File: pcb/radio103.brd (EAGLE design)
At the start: 99 x 98.7 mm, 11 parts, among them IC1 LM833D, IC2 LM833D, IC3 74ACT00D, IC4 MCP23S17SO, IC5 LM386M-1, U1 FST3253

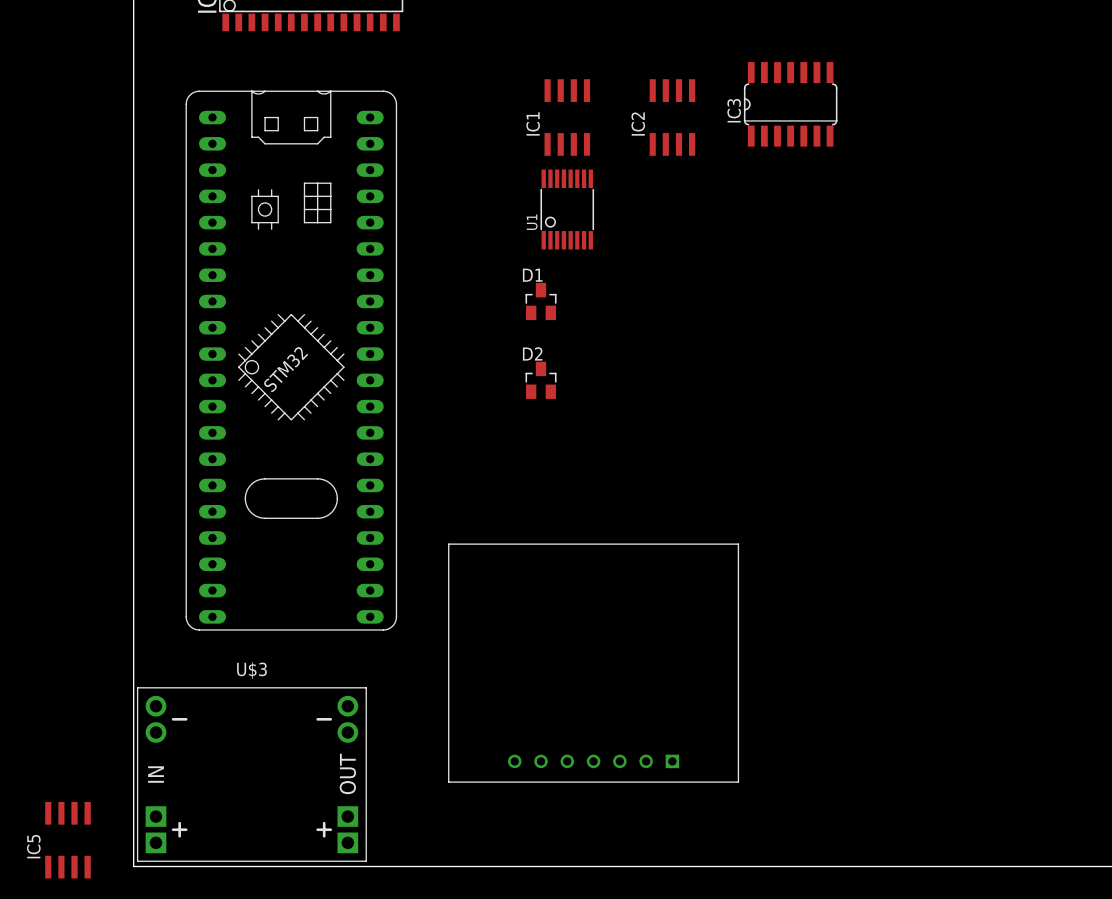
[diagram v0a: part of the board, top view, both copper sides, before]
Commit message: AGC + soft clipper
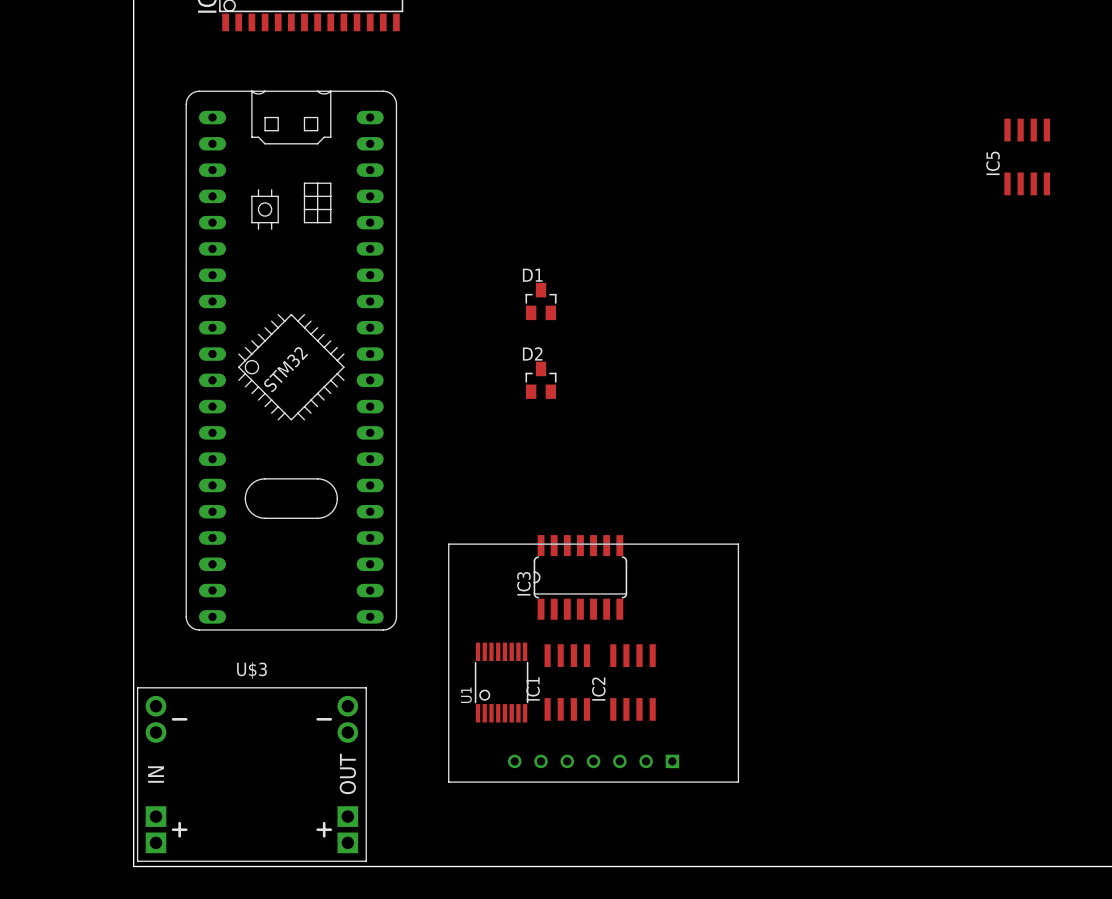
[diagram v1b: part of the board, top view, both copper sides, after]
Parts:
- moved IC5 113.8 mm to (86.4, 68.6)
- moved IC2 54.7 mm to (48.3, 17.8)
- moved IC1 54.6 mm to (41.9, 17.8)
- moved IC3 50.0 mm to (43.2, 27.9)
- moved U1 46.2 mm to (35.6, 17.8)
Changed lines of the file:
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@@
 </layers>
 <board>
+<fusionsync huburn="a.cGVyc29uYWw6dWUyYzhiYjNk" projecturn="a.cGVyc29uYWw6dWUyYzhiYjNkIzIwMTkwMTI3MTcyNzM0MDc2" f3durn="urn:adsk.wipprod:dm.lineage:HAib8JV9QH6EPJWf0lSnAA" pcbguid="9a40abf5-9ee6-4638-9549-066028e06783" lastpulledtime="" lastsyncedchangeguid="" latestrevisionid="0aad2595-9f46-4cf1-a5a6-6076ba2b8e60" lastsyncedrevisionid="0aad2595-9f46-4cf1-a5a6-6076ba2b8e60" lastboardhashguid="17746136-b05b-aa1b-f81e-0eeb9cca154b" lastpushedtime="2022-06-26T19:07:11Z" linktopcb3d="true"/>
 <plain>
 <wire x1="0" y1="0" x2="99.04" y2="0" width="0" layer="20"/>
@@
 <attribute name="VALUE" x="11.43" y="-0.635" size="1.27" layer="27" align="top-center"/>
 </element>
-<element name="IC1" library="linear" library_urn="urn:adsk.eagle:library:262" package="SO08" package3d_urn="urn:adsk.eagle:package:16404/2" value="LM833D" x="41.91" y="72.39" smashed="yes">
-<attribute name="NAME" x="39.243" y="70.485" size="1.27" layer="25" rot="R90"/>
-<attribute name="POPULARITY" value="0" x="31.75" y="106.68" size="1.778" layer="27" display="off"/>
-<attribute name="VALUE" x="45.847" y="70.485" size="1.27" layer="27" rot="R90"/>
-</element>
-<element name="IC2" library="linear" library_urn="urn:adsk.eagle:library:262" package="SO08" package3d_urn="urn:adsk.eagle:package:16404/2" value="LM833D" x="52.07" y="72.39" smashed="yes">
-<attribute name="NAME" x="49.403" y="70.485" size="1.27" layer="25" rot="R90"/>
-<attribute name="POPULARITY" value="0" x="21.59" y="106.68" size="1.778" layer="27" display="off"/>
-<attribute name="VALUE" x="56.007" y="70.485" size="1.27" layer="27" rot="R90"/>
-</element>
-<element name="U1" library="ub0baa" package="TSSOP16L" value="FST3253" x="41.91" y="63.5" smashed="yes">
-<attribute name="NAME" x="39.0144" y="61.4172" size="1.016" layer="25" ratio="10" rot="R90"/>
-<attribute name="VALUE" x="45.7962" y="61.4172" size="1.016" layer="27" ratio="10" rot="R90"/>
-</element>
-<element name="IC3" library="74xx-eu" library_urn="urn:adsk.eagle:library:85" package="SO14" package3d_urn="urn:adsk.eagle:package:1010/2" value="74ACT00D" x="63.5" y="73.66" smashed="yes">
-<attribute name="NAME" x="58.674" y="71.755" size="1.27" layer="25" ratio="10" rot="R90"/>
-<attribute name="POPULARITY" value="0" x="24.13" y="88.9" size="1.778" layer="27" display="off"/>
-<attribute name="VALUE" x="60.325" y="72.898" size="1.27" layer="27" ratio="10"/>
+<element name="IC1" library="linear" library_urn="urn:adsk.eagle:library:262" package="SO08" package3d_urn="urn:adsk.eagle:package:16404/2" value="LM833D" x="41.91" y="17.78" smashed="yes">
+<attribute name="NAME" x="39.243" y="15.875" size="1.27" layer="25" rot="R90"/>
+<attribute name="POPULARITY" value="0" x="31.75" y="52.07" size="1.778" layer="27" display="off"/>
+<attribute name="VALUE" x="45.847" y="15.875" size="1.27" layer="27" rot="R90"/>
+</element>
+<element name="IC2" library="linear" library_urn="urn:adsk.eagle:library:262" package="SO08" package3d_urn="urn:adsk.eagle:package:16404/2" value="LM833D" x="48.26" y="17.78" smashed="yes">
+<attribute name="NAME" x="45.593" y="15.875" size="1.27" layer="25" rot="R90"/>
+<attribute name="POPULARITY" value="0" x="17.78" y="52.07" size="1.778" layer="27" display="off"/>
+<attribute name="VALUE" x="52.197" y="15.875" size="1.27" layer="27" rot="R90"/>
+</element>
+<element name="U1" library="ub0baa" package="TSSOP16L" value="FST3253" x="35.56" y="17.78" smashed="yes">
+<attribute name="NAME" x="32.6644" y="15.6972" size="1.016" layer="25" ratio="10" rot="R90"/>
+<attribute name="VALUE" x="39.4462" y="15.6972" size="1.016" layer="27" ratio="10" rot="R90"/>
+</element>
+<element name="IC3" library="74xx-eu" library_urn="urn:adsk.eagle:library:85" package="SO14" package3d_urn="urn:adsk.eagle:package:1010/2" value="74ACT00D" x="43.18" y="27.94" smashed="yes">
+<attribute name="NAME" x="38.354" y="26.035" size="1.27" layer="25" ratio="10" rot="R90"/>
+<attribute name="POPULARITY" value="0" x="3.81" y="43.18" size="1.778" layer="27" display="off"/>
+<attribute name="VALUE" x="49.022" y="23.495" size="1.27" layer="27" ratio="10" rot="R90"/>
 </element>
 <element name="U$2" library="ub0baa" package="CJMCU-5351" value="CJMCU-5351" x="44.45" y="10.16" smashed="yes"/>
@@
 <attribute name="VALUE" x="37.465" y="43.815" size="1.27" layer="27"/>
 </element>
-<element name="IC5" library="linear" library_urn="urn:adsk.eagle:library:262" package="SO08" package3d_urn="urn:adsk.eagle:package:16404/2" value="LM386M-1" x="-6.35" y="2.54" smashed="yes">
-<attribute name="NAME" x="-9.017" y="0.635" size="1.27" layer="25" rot="R90"/>
-<attribute name="POPULARITY" value="0" x="-6.35" y="2.54" size="1.778" layer="27" display="off"/>
-<attribute name="VALUE" x="-2.413" y="0.635" size="1.27" layer="27" rot="R90"/>
+<element name="IC5" library="linear" library_urn="urn:adsk.eagle:library:262" package="SO08" package3d_urn="urn:adsk.eagle:package:16404/2" value="LM386M-1" x="86.36" y="68.58" smashed="yes">
+<attribute name="NAME" x="83.693" y="66.675" size="1.27" layer="25" rot="R90"/>
+<attribute name="POPULARITY" value="0" x="86.36" y="68.58" size="1.778" layer="27" display="off"/>
+<attribute name="VALUE" x="90.297" y="65.405" size="1.27" layer="27" rot="R90"/>
 </element>
 </elements>
@@
 <contactref element="IC1" pad="8"/>
 <contactref element="IC2" pad="8"/>
-<wire x1="50.165" y1="74.99" x2="40.005" y2="74.99" width="0" layer="19" extent="1-1"/>
+<wire x1="46.355" y1="20.38" x2="40.005" y2="20.38" width="0" layer="19" extent="1-1"/>
 </signal>
 <signal name="V-">
 <contactref element="IC1" pad="4"/>
 <contactref element="IC2" pad="4"/>
-<wire x1="53.975" y1="69.79" x2="43.815" y2="69.79" width="0" layer="19" extent="1-1"/>
+<wire x1="50.165" y1="15.18" x2="43.815" y2="15.18" width="0" layer="19" extent="1-1"/>
 </signal>
 <signal name="GND">
 <contactref element="IC3" pad="7"/>
 <contactref element="IC5" pad="4"/>
-<wire x1="-4.445" y1="-0.06" x2="67.31" y2="70.5866" width="0" layer="19" extent="1-1"/>
+<wire x1="88.265" y1="65.98" x2="46.99" y2="24.8666" width="0" layer="19" extent="1-1"/>
 </signal>
 <signal name="VCC">
@@
 </note>
 <note version="8.3" severity="warning">
+Since Version 8.3, EAGLE supports Fusion synchronisation.
+This feature will not be available in this version and saving
+the document will break the link to the Fusion PCB feature.
+</note>
+<note version="8.3" severity="warning">

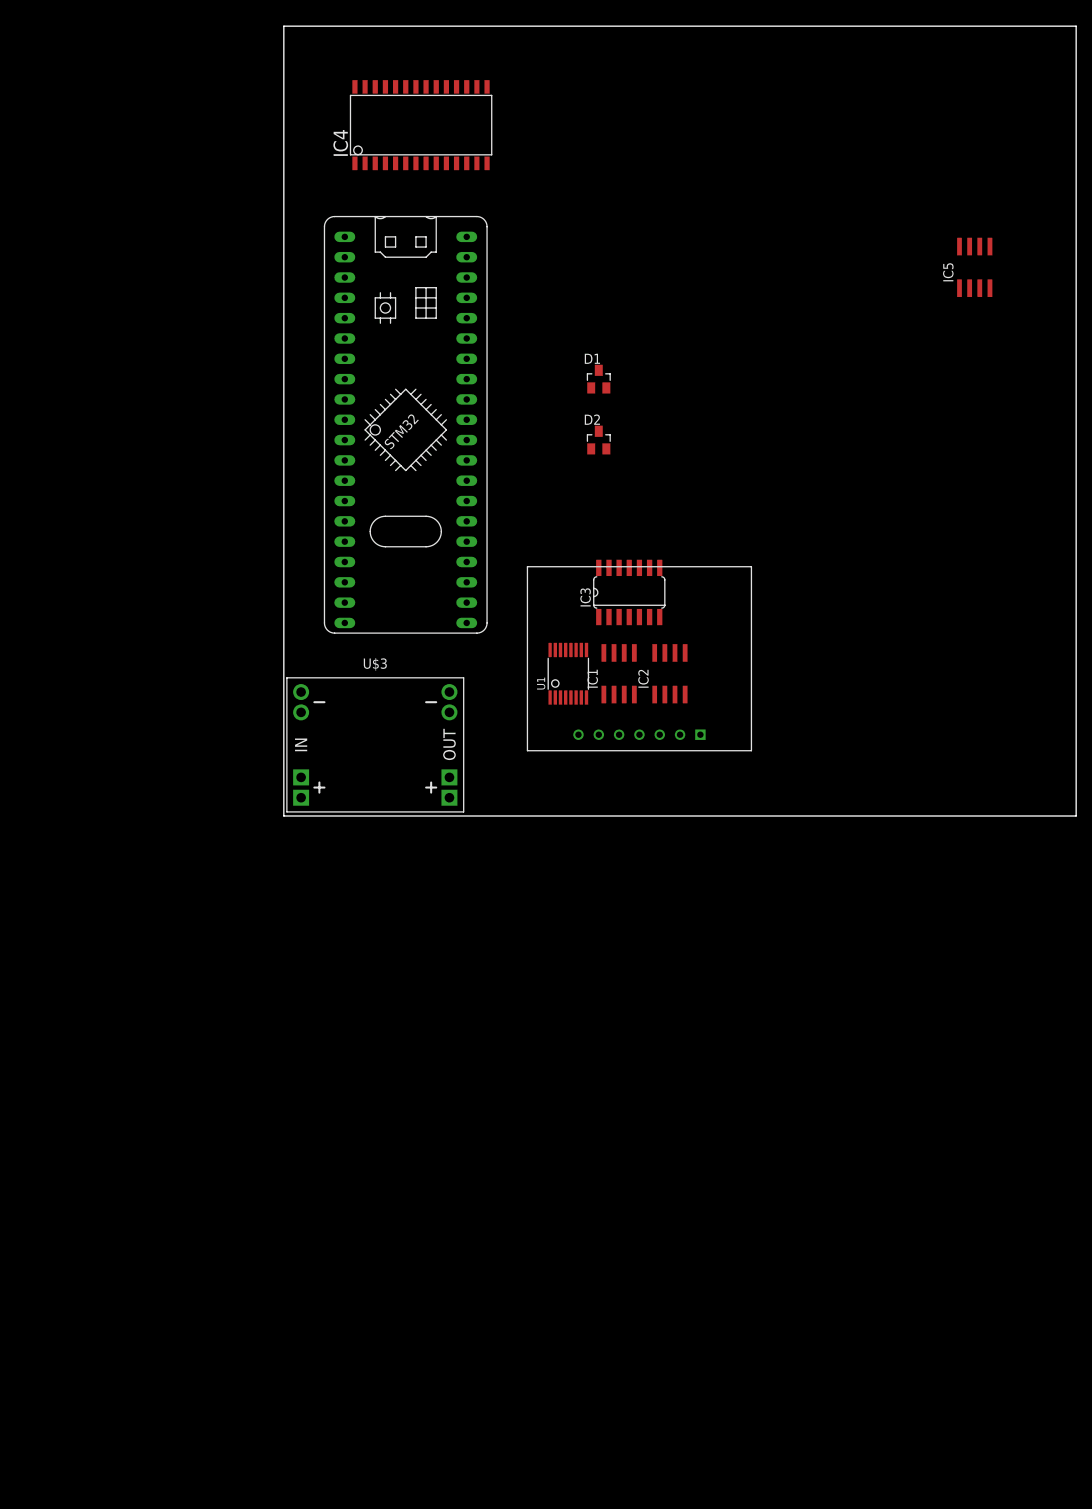
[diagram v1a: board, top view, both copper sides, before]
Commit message: MCP23S17 + CD4066 + decimation works!
don't use remapped SPI1 w/ I2C1!
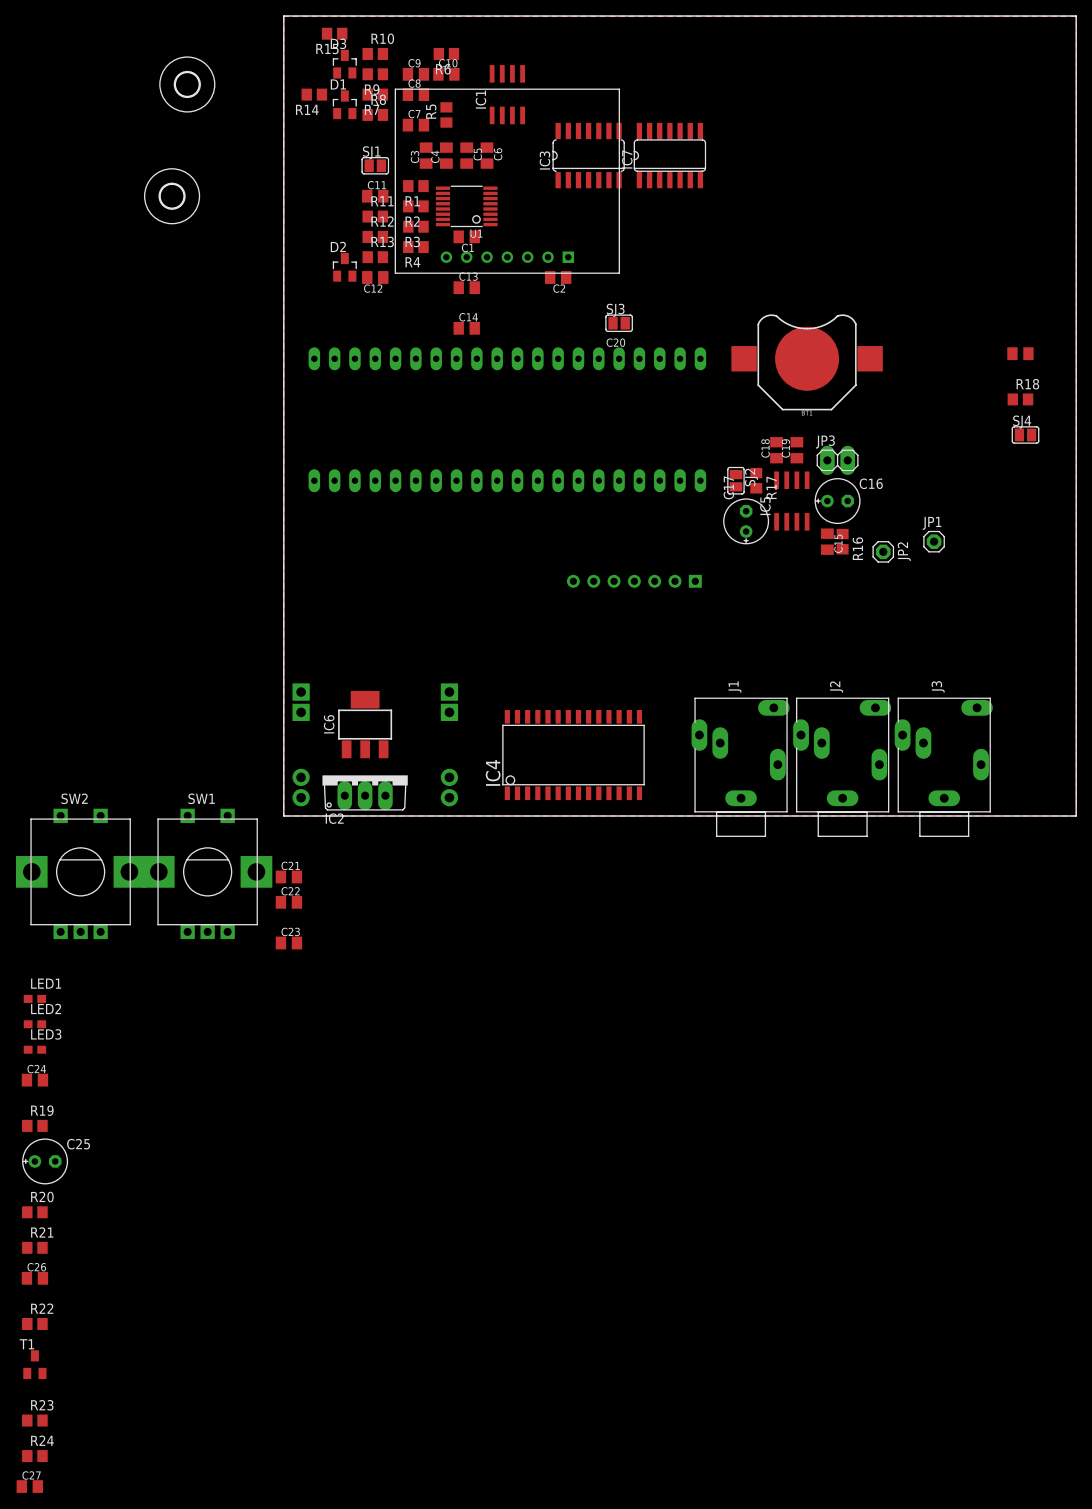
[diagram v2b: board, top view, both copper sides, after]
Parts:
- added BT1: (no value), SparkFun-Batteries:BATTCON_12MM
- added C1, C10, C11, C12, C13, C14, C15, C18, C19, C2, C20, C21, C22, C23, C24, C26, C27, C3, C4, C5, C6, C7, C8, C9: 100n, rcl:C0805K
- added C16, C17, C25: (no value), rcl:E2,5-6E
- added D3: BAT54S, diode:SOT23
- added H1, H2: MOUNT-HOLE3.0, holes:3,0
- added IC6: LM1117MPX-3.3, lm1117:SOT223
- added IC7: 4066D, 40xx:SO14
- added J1, J2, J3: PJ-324MH, ub0baa:PJ-324MH
- added JP1, JP2: (no value), pinhead:1X01
- added JP3: (no value), pinhead:1X02
- added LED1, LED2, LED3: (no value), led-smd:C1608
- added R1, R10, R11, R12, R13, R14, R15, R16, R17, R18, R19, R2, R20, R21, R22, R23, R24, R3, R4, R5, R6, R7, R8, R9: (no value), rcl:R0805
- added SJ1, SJ2, SJ3, SJ4: (no value), jumper:SJ
- added SW1, SW2: EC12E_SW, switch-alps:ALPS_EC12E_SW
- added T1: BC847, transistor:SOT23
- added U$4: SSD1309_2.4_OLED, ub0baa:SSD1309_2.42_OLED
- IC2: value LM833D -> 7805TV; device linear:SO08 -> linear:TO220V
- moved IC4 81.0 mm to (35.6, 7.62)
- moved IC1 73.7 mm to (27.9, 90.2)
- moved U$2 61.9 mm to (27.9, 69.8)
- moved U1 59.8 mm to (22.9, 76.2), turned to 90 degrees
- moved IC3 54.8 mm to (38.1, 82.5)
- moved D1 46.7 mm to (7.62, 88.9)
- moved IC2 40.2 mm to (10.2, 5.08)
- moved D2 38.4 mm to (7.62, 68.6)
- moved IC5 37.1 mm to (63.5, 39.4)
- moved U$1 8.52 mm to (19.1, 49.5), flipped to the bottom, turned to 270 degrees
- flipped U$3 to the bottom, turned to 180 degrees
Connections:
- removed net V+: IC1.8, IC2.8
- removed net V-: IC1.4, IC2.4
- removed net VCC: IC3.14
- removed net VS: IC5.6
- new net 3V3: C1.2, C13.2, C2.2, C22.2, C27.2, D1.2, D3.2, IC3.14, IC4.9, IC6.2, IC6.TAB, R12.2, R23.2, R7.2, R9.2, U$2.VIN, U$4.VCC, U1.16
- new net 5V: C19.1, C23.2, IC2.3, IC5.6, IC6.3, U$3.OUT-.1, U$3.OUT-.2
- new net ADC_BTN: U$1.A3
- new net ADC_I1: C8.1, D1.3, R14.1, R7.1, R8.2
- new net ADC_MIC: U$1.A2
- new net ADC_Q1: C9.1, D3.3, R10.2, R15.1, R9.1
- new net ADC_RX_I: IC7.2, IC7.9, U$1.A0
- new net ADC_RX_Q: IC7.10, IC7.3, U$1.A1
- new net ADC_SWR_F: U$1.A4
- new net ADC_SWR_R: U$1.A5
- new net ADC_VIN: U$1.A6
- new net AUDIO: IC5.3
- new net AUDIO_PWM: U$1.A10
- new net EXP_CS: IC4.11
- new net LCD_CS: U$4.CS
- new net LCD_DC: U$4.DC
- new net LCD_RES: U$4.RES
- new net MIC: IC7.8
- new net N$1: C3.1, R1.1, U1.10
- new net N$10: C7.1, C8.2, IC1.7, R5.2
- new net N$12: C11.2, R11.2, U1.9
- new net N$13: U$2.1, U1.2
- new net N$14: C12.2, R11.1, R12.1, R13.1
- new net N$15: U$2.0, U1.14
- new net N$16: IC4.21, SW1.B
- new net N$17: IC3.8, U1.6
- new net N$18: IC3.11, U1.5
- new net N$19: C17.+, IC5.1
- new net N$2: C4.1, R2.1, U1.11
- new net N$20: IC5.8, R17.1, SJ2.1
- new net N$21: C17.-, R17.2, SJ2.2
- new net N$22: C18.1, IC5.7
- new net N$23: C16.+, IC5.5
- new net N$24: C15.1, C16.-, JP3.1
- new net N$25: C15.2, R16.2
- new net N$26: IC3.2, SJ1.2, U$2.2
- new net N$27: IC3.1, SJ1.1, SJ4.2
- new net N$28: IC3.3, IC3.5, SJ3.2
- new net N$29: IC3.4, SJ3.1
- new net N$3: C5.2, R3.1, U1.12
- new net N$30: C20.2, IC3.6, R18.1
- new net N$31: SJ4.1, U1.7
- new net N$32: C25.-, R20.2, R21.2
- new net N$33: C24.1, R21.1, R22.2
- new net N$34: C26.1, R22.1
- new net N$35: C25.+
- new net N$36: BT1.PWR@1, R19.1
- new net N$37: R19.2, U$1.VBAT
- new net N$38: IC4.22, SW1.A
- new net N$39: R24.1, T1.1
- new net N$4: C6.2, R4.1, U1.13
- new net N$40: IC4.23, SW2.B
- new net N$41: IC4.24, SW2.A
- new net N$5: C10.2, IC1.2, R1.2, R6.1
- new net N$6: IC1.5, R2.2
- new net N$7: C7.2, IC1.6, R3.2, R5.1
- new net N$8: IC1.3, R4.2
- new net N$9: C10.1, C9.2, IC1.1, R6.2
- new net ONBOARD_LED: U$1.C13
- new net RESET: IC4.18
- new net RTC_OSC_IN: U$1.C14
- new net RTC_OSC_OUT: U$1.C15
- new net RX: C11.1
- new net RXEN: IC7.13, IC7.5, R24.2
- new net RX_I: IC7.1, R14.2
- new net RX_Q: IC7.4, R15.2
- new net SCL: U$1.B8, U$2.SCL
- new net SDA: U$1.B9, U$2.SDA
- new net SPI_MISO: IC4.14, U$1.B4
- new net SPI_MOSI: IC4.13, U$1.B5, U$4.SDA
- new net SPI_SCK: IC4.12, U$1.B3, U$4.SCK
- new net TX: C20.1, R18.2
- new net TXEN: IC7.12, IC7.6, R23.1, T1.3
- new net TX_I: IC3.12, IC3.13, U1.3
- new net TX_I_PWM: U$1.A8
- new net TX_Q: IC3.10, IC3.9, U1.4
- new net TX_Q_PWM: U$1.A11
- new net UART_RX: U$1.B7
- new net UART_TX: U$1.B6
- new net VIN: C21.2, IC2.1, U$3.IN-.1, U$3.IN-.2
- new net VOPAMP: C14.2, IC1.8
- net GND: now also BT1.GND, C1.1, C12.1, C13.1, C14.1, C18.2, C19.2, C2.1, C21.1, C22.1, C23.1, C24.2, C26.2, C27.1, C3.2, C4.2, C5.1, C6.1, D1.1, D3.1, IC1.4, IC2.2, IC4.10, IC4.15, IC4.16, IC4.17, IC5.2, IC6.1, IC7.11, JP3.2, R10.1, R13.2, R16.1, R20.1, R8.1, SW1.C, SW2.C, T1.2, U$2.GND, U$3.IN+.1, U$3.IN+.2, U$3.OUT+.1, U$3.OUT+.2, U$4.GND, U1.1, U1.15, U1.8
- net VDD: now also IC7.14; no longer IC4.9
- net VSS: now also IC7.7; no longer IC4.10
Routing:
- added copper zone on layer 1, net GND
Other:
- board size 99 x 98.7 mm -> 99 x 100 mm
